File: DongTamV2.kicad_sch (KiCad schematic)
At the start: 13 parts, among them J1 KF128, J2 KF128, J3 KF128, J4 KF128, J5 KF128

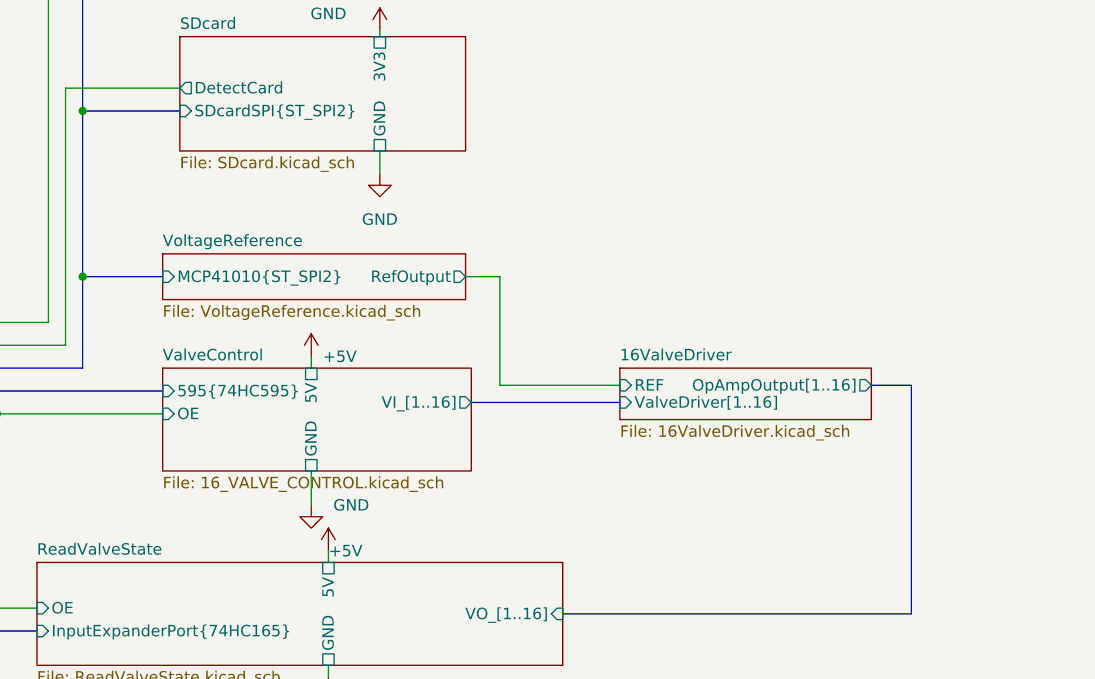
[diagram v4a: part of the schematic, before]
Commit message: Layout p2, fix Analog VCC and GND for opamp circuit
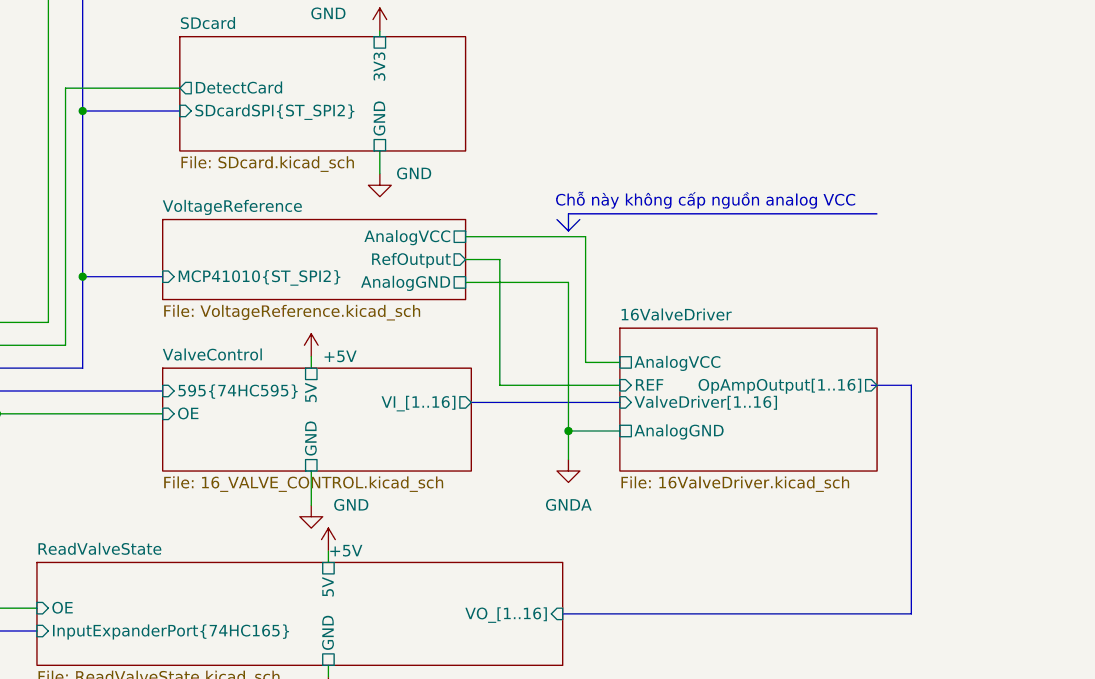
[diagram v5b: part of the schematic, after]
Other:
- sheet 16ValveDriver ports: added AnalogGND, AnalogVCC; removed none
- sheet VoltageReference ports: added AnalogGND, AnalogVCC; removed none
- note added: "Chỗ này không cấp nguồn analog VCC"
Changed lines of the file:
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@@
 	)
 	(junction
+		(at 209.55 131.445)
+		(diameter 0)
+		(color 0 0 0 0)
+	)
+	(junction
 		(at 58.42 27.94)
 		(diameter 0)
@@
 	(wire
 		(pts
+			(xy 209.55 131.445) (xy 209.55 134.62)
+		)
+		(stroke
+			(width 0)
+			(type default)
+		)
+	)
+	(wire
+		(pts
 			(xy 180.975 123.19) (xy 180.975 124.46)
 		)
@@
 		)
 	)
+	(polyline
+		(pts
+			(xy 209.55 107.315) (xy 209.55 109.22)
+		)
+		(stroke
+			(width 0)
+			(type default)
+		)
+	)
 	(wire
 		(pts
@@
 		)
 	)
+	(polyline
+		(pts
+			(xy 243.84 107.315) (xy 209.55 107.315)
+		)
+		(stroke
+			(width 0)
+			(type default)
+		)
+	)
 	(wire
 		(pts
@@
 	(wire
 		(pts
+			(xy 211.455 109.855) (xy 211.455 123.825)
+		)
+		(stroke
+			(width 0)
+			(type default)
+		)
+	)
+	(wire
+		(pts
 			(xy 62.865 33.655) (xy 69.215 33.655)
 		)
@@
 		)
 	)
+	(wire
+		(pts
+			(xy 211.455 123.825) (xy 215.265 123.825)
+		)
+		(stroke
+			(width 0)
+			(type default)
+		)
+	)
 	(bus
 		(pts
@@
 	(wire
 		(pts
+			(xy 215.265 131.445) (xy 209.55 131.445)
+		)
+		(stroke
+			(width 0)
+			(type default)
+		)
+	)
+	(wire
+		(pts
 			(xy 58.42 27.94) (xy 69.215 27.94)
 		)
@@
 		)
 	)
+	(polyline
+		(pts
+			(xy 209.55 109.22) (xy 210.82 107.95)
+		)
+		(stroke
+			(width 0)
+			(type default)
+		)
+	)
 	(bus
 		(pts
@@
 	(wire
 		(pts
-			(xy 201.93 114.3) (xy 198.12 114.3)
+			(xy 201.93 112.395) (xy 198.12 112.395)
 		)
 		(stroke
@@
 	(wire
 		(pts
+			(xy 198.12 114.935) (xy 209.55 114.935)
+		)
+		(stroke
+			(width 0)
+			(type default)
+		)
+	)
+	(wire
+		(pts
 			(xy 39.37 43.18) (xy 39.37 45.72)
 		)
@@
 	(wire
 		(pts
-			(xy 201.93 126.365) (xy 201.93 114.3)
+			(xy 201.93 126.365) (xy 201.93 112.395)
 		)
 		(stroke
@@
 	(wire
 		(pts
+			(xy 209.55 114.935) (xy 209.55 131.445)
+		)
+		(stroke
+			(width 0)
+			(type default)
+		)
+	)
+	(polyline
+		(pts
+			(xy 208.28 107.95) (xy 209.55 109.22)
+		)
+		(stroke
+			(width 0)
+			(type default)
+		)
+	)
+	(wire
+		(pts
 			(xy 153.67 31.75) (xy 160.655 31.75)
 		)
@@
 		)
 	)
+	(wire
+		(pts
+			(xy 198.12 109.855) (xy 211.455 109.855)
+		)
+		(stroke
+			(width 0)
+			(type default)
+		)
+	)
 	(bus
 		(pts
@@
 		)
 	)
+	(text "Chỗ này không cấp nguồn analog VCC"
+		(exclude_from_sim no)
+		(at 224.79 106.045 0)
+		(effects
+			(font
+				(size 1.27 1.27)
+			)
+		)
+	)
 	(text "For external DC supply if 220V is not used"
 		(exclude_from_sim no)
@@
 		(on_board yes)
 		(dnp no)
-		(fields_autoplaced yes)
 		(property "Reference" "#PWR020"
 			(at 188.595 109.22 0)
@@
 		)
 		(property "Value" "GND"
-			(at 188.595 107.95 0)
+			(at 192.405 102.87 0)
 			(effects
 				(font
@@
 	)
 	(symbol
+		(lib_id "power:GNDA")
+		(at 209.55 134.62 0)
+		(unit 1)
+		(exclude_from_sim no)
+		(in_bom yes)
+		(on_board yes)
+		(dnp no)
+		(fields_autoplaced yes)
+		(property "Reference" "#PWR050"
+			(at 209.55 140.97 0)
+			(effects
+				(font
+					(size 1.27 1.27)
+				)
+				(hide yes)
+			)
+		)
+		(property "Value" "GNDA"
+			(at 209.55 139.7 0)
+			(effects
+				(font
+					(size 1.27 1.27)
+				)
+			)
+		)
+		(property "Footprint" ""
+			(at 209.55 134.62 0)
+			(effects
+				(font
+					(size 1.27 1.27)
+				)
+				(hide yes)
+			)
+		)
+		(property "Datasheet" ""
+			(at 209.55 134.62 0)
+			(effects
+				(font
+					(size 1.27 1.27)
+				)
+				(hide yes)
+			)
+		)
+		(property "Description" "Power symbol creates a global label with name \"GNDA\" , analog ground"
+			(at 209.55 134.62 0)
+			(effects
+				(font
+					(size 1.27 1.27)
+				)
+				(hide yes)
+			)
+		)
+		(pin "1"
+		)
+		(instances
+			(project "DongTamV2"
+				(path "/2303d546-b88a-4ab0-aee1-26e3b32ac9d7"
+					(reference "#PWR050")
+					(unit 1)
+				)
+			)
+		)
+	)
+	(symbol
 		(lib_id "power:GND")
 		(at 39.37 45.72 0)
@@
 	)
 	(sheet
-		(at 215.265 124.46)
-		(size 27.94 5.715)
+		(at 215.265 120.015)
+		(size 28.575 15.875)
 		(fields_autoplaced yes)
 		(stroke
@@
 		)
 		(property "Sheetname" "16ValveDriver"
-			(at 215.265 123.7484 0)
+			(at 215.265 119.3034 0)
 			(effects
 				(font
@@
 		)
 		(property "Sheetfile" "16ValveDriver.kicad_sch"
-			(at 215.265 130.7596 0)
+			(at 215.265 136.4746 0)
 			(effects
 				(font
@@
 		)
 		(property "Field2" ""
-			(at 215.265 124.46 0)
+			(at 215.265 120.015 0)
 			(effects
 				(font
@@
 		)
 		(pin "OpAmpOutput[1..16]" output
-			(at 243.205 126.365 0)
+			(at 243.84 126.365 0)
 			(effects
 				(font
@@
 			)
 		)
+		(pin "AnalogGND" passive
+			(at 215.265 131.445 180)
+			(effects
+				(font
+					(size 1.27 1.27)
+				)
+				(justify left)
+			)
+		)
+		(pin "AnalogVCC" passive
+			(at 215.265 123.825 180)
+			(effects
+				(font
+					(size 1.27 1.27)
+				)
+				(justify left)
+			)
+		)
 		(instances
 			(project "DongTamV2"
@@
 	)
 	(sheet
-		(at 164.465 111.76)
-		(size 33.655 5.08)
+		(at 164.465 107.95)
+		(size 33.655 8.89)
 		(fields_autoplaced yes)
 		(stroke
@@
 		)
 		(property "Sheetname" "VoltageReference"
-			(at 164.465 111.0484 0)
+			(at 164.465 107.2384 0)
 			(effects
 				(font
@@
 		)
 		(property "Field2" ""
-			(at 164.465 111.76 0)
+			(at 164.465 107.95 0)
 			(effects
 				(font
@@
 		)
 		(pin "RefOutput" output
-			(at 198.12 114.3 0)
+			(at 198.12 112.395 0)
 			(effects
 				(font
@@
 			)
 		)
+		(pin "AnalogGND" passive
+			(at 198.12 114.935 0)
+			(effects
+				(font
+					(size 1.27 1.27)
+				)
+				(justify right)
+			)
+		)
+		(pin "AnalogVCC" passive
+			(at 198.12 109.855 0)
+			(effects
+				(font
+					(size 1.27 1.27)
+				)
+				(justify right)
+			)
+		)

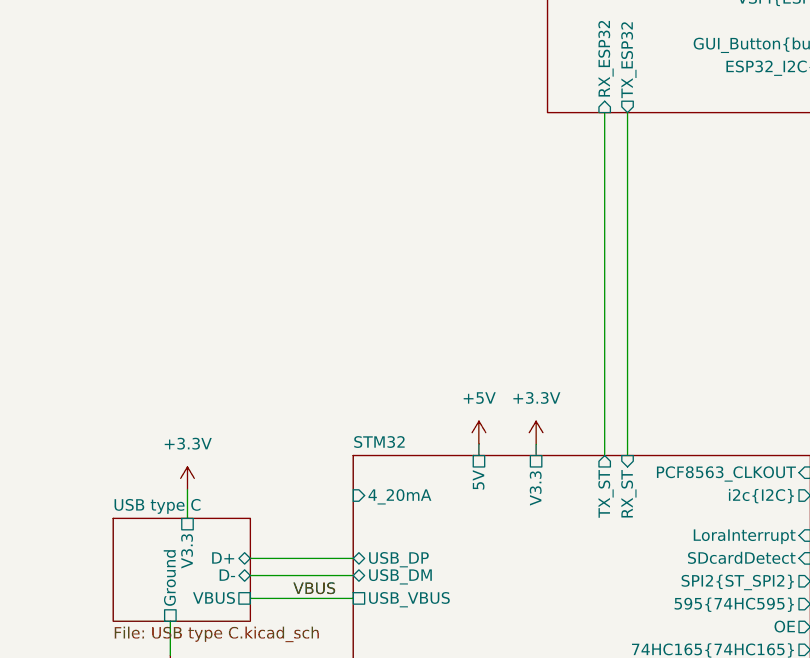
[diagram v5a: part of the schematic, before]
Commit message: feat: adding HW685 module
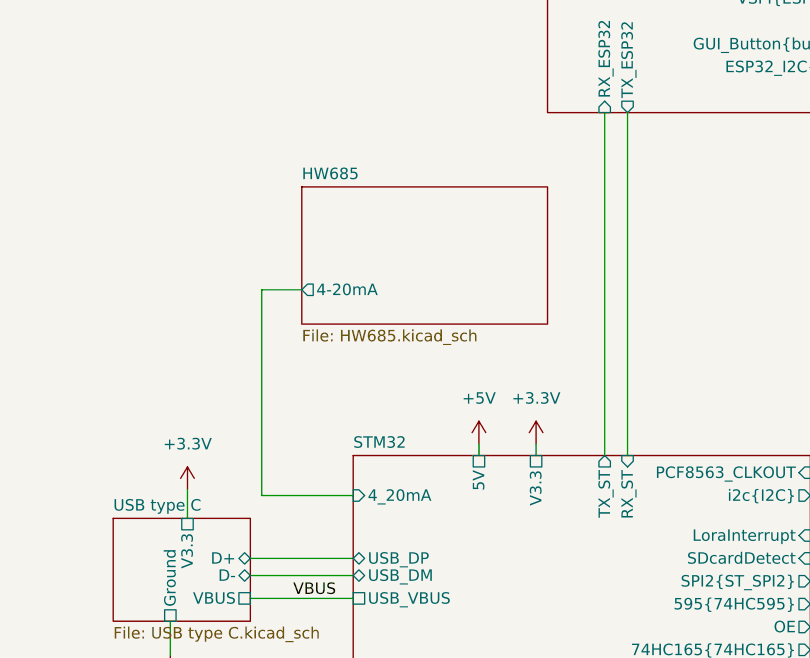
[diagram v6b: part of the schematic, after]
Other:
- added sheet HW685 (HW685.kicad_sch)
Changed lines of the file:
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@@
 		)
 	)
+	(wire
+		(pts
+			(xy 47.625 92.075) (xy 43.18 92.075)
+		)
+		(stroke
+			(width 0)
+			(type default)
+		)
+	)
 	(bus
 		(pts
@@
 	(wire
 		(pts
+			(xy 43.18 114.935) (xy 53.34 114.935)
+		)
+		(stroke
+			(width 0)
+			(type default)
+		)
+	)
+	(wire
+		(pts
 			(xy 41.91 126.365) (xy 53.34 126.365)
 		)
@@
 	(wire
 		(pts
+			(xy 43.18 92.075) (xy 43.18 114.935)
+		)
+		(stroke
+			(width 0)
+			(type default)
+		)
+	)
+	(wire
+		(pts
 			(xy 63.5 140.97) (xy 63.5 142.24)
 		)
@@
 				)
 			)
+		)
+	)
+	(sheet
+		(at 47.625 80.645)
+		(size 27.305 15.24)
+		(fields_autoplaced yes)
+		(stroke
+			(width 0.1524)
+			(type solid)
+		)
+		(fill
+			(color 15 122 255 1.0000)
+		)
+		(property "Sheetname" "HW685"
+			(at 47.625 79.9334 0)
+			(effects
+				(font
+					(size 1.27 1.27)
+				)
+				(justify left bottom)
+			)
+		)
+		(property "Sheetfile" "HW685.kicad_sch"
+			(at 47.625 96.4696 0)
+			(effects
+				(font
+					(size 1.27 1.27)
+				)
+				(justify left top)
+			)
+		)
+		(pin "4-20mA" output
+			(at 47.625 92.075 180)
+			(effects
+				(font
+					(size 1.27 1.27)
+				)
+				(justify left)
+			)
+		)
+		(instances
+			(project "DongTamV2"
+				(path "/2303d546-b88a-4ab0-aee1-26e3b32ac9d7"
+					(page "23")
+				)
+			)
